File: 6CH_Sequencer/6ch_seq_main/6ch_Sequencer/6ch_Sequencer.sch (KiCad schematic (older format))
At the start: 38 parts, among them J1 CH1, J1 POWER, J2 CH2, J3 CH3, J4 CH4, J5 CH5, J6 CH6, J7 CLOCK_IN, SW1 SW_Push, SW2 Rotary_Encoder

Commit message: addPCB
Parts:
- A1: footprint Module:Arduino_Nano -> Arduino:Arduino_Nano
- J1, J2, J3, J4, J5, J6, J7: footprint (none) -> Connector_Audio:Jack_3.5mm_QingPu_WQP-PJ398SM_Vertical_CircularHoles
- J8: renamed from J1; footprint (none) -> Connector_IDC:IDC-Header_2x05_P2.54mm_Vertical
- SW1: footprint Buttons_Switches_THT:SW_PUSH-12mm -> digikey-footprints:Toggle_Switch_100SP1T1B4M2QE
- SW2: footprint Rotary_Encoder:RotaryEncoder_Alps_EC12E_Vertical_H20mm -> digikey-footprints:Rotary_Encoder_Switched_PEC11R

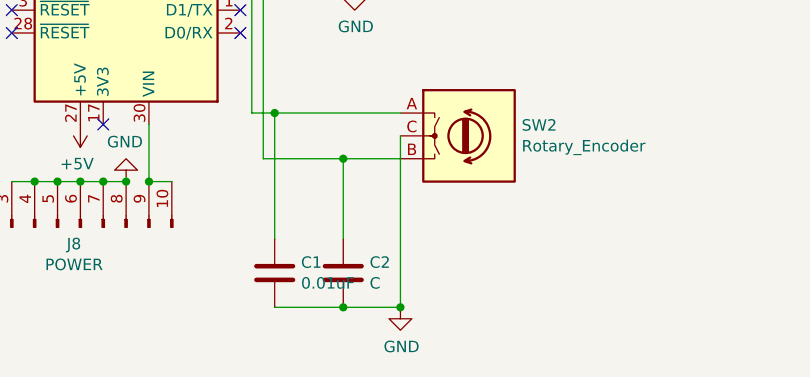
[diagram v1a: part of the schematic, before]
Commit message: addBOM
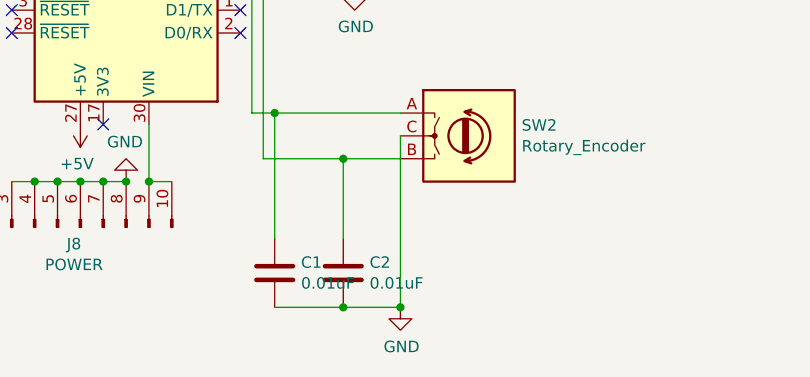
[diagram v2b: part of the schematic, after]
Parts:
- C2: value C -> 0.01uF
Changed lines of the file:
@@
 P 5050 5950
 F 0 "C2" H 5165 5996 50  0000 L CNN
-F 1 "C" H 5165 5905 50  0000 L CNN
+F 1 "0.01uF" H 5165 5905 50  0000 L CNN
 F 2 "Capacitors_THT:C_Disc_D5.0mm_W2.5mm_P5.00mm" H 5088 5800 50  0001 C CNN
 F 3 "~" H 5050 5950 50  0001 C CNN

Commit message: AddNewFile
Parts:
- Brd1: symbol SSD1306-128x64_OLED:SSD1306 -> 6ch_Sequencer-rescue:SSD1306-SSD1306-128x64_OLED
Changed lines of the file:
@@
 $EndComp
 $Comp
-L SSD1306-128x64_OLED:SSD1306 Brd1
+L 6ch_Sequencer-rescue:SSD1306-SSD1306-128x64_OLED Brd1
 U 1 1 606D4D59
 P 2700 4350
